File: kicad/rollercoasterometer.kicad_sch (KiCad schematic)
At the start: 15 parts, among them J101 USB_C_Receptacle, J120 STANDOFF, J125 STANDOFF, J127 STANDOFF, J129 STANDOFF, U104 Teensy4.1

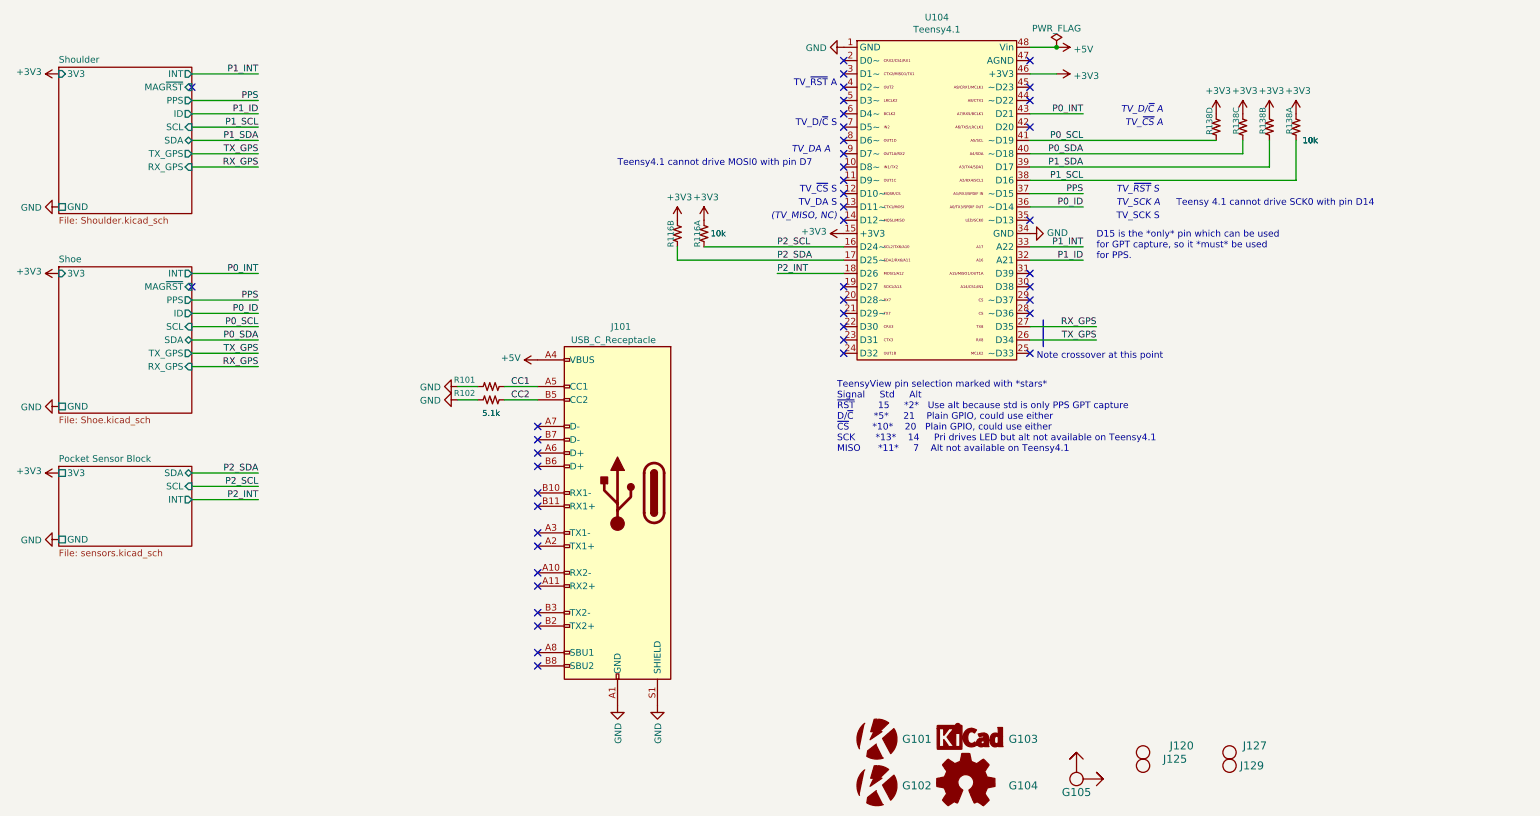
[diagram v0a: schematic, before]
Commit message: Added reference to TeensyView
TeensyView does not get a footprint because it mounts on top of the Teensy, but it is hooked up to the schematic properly.
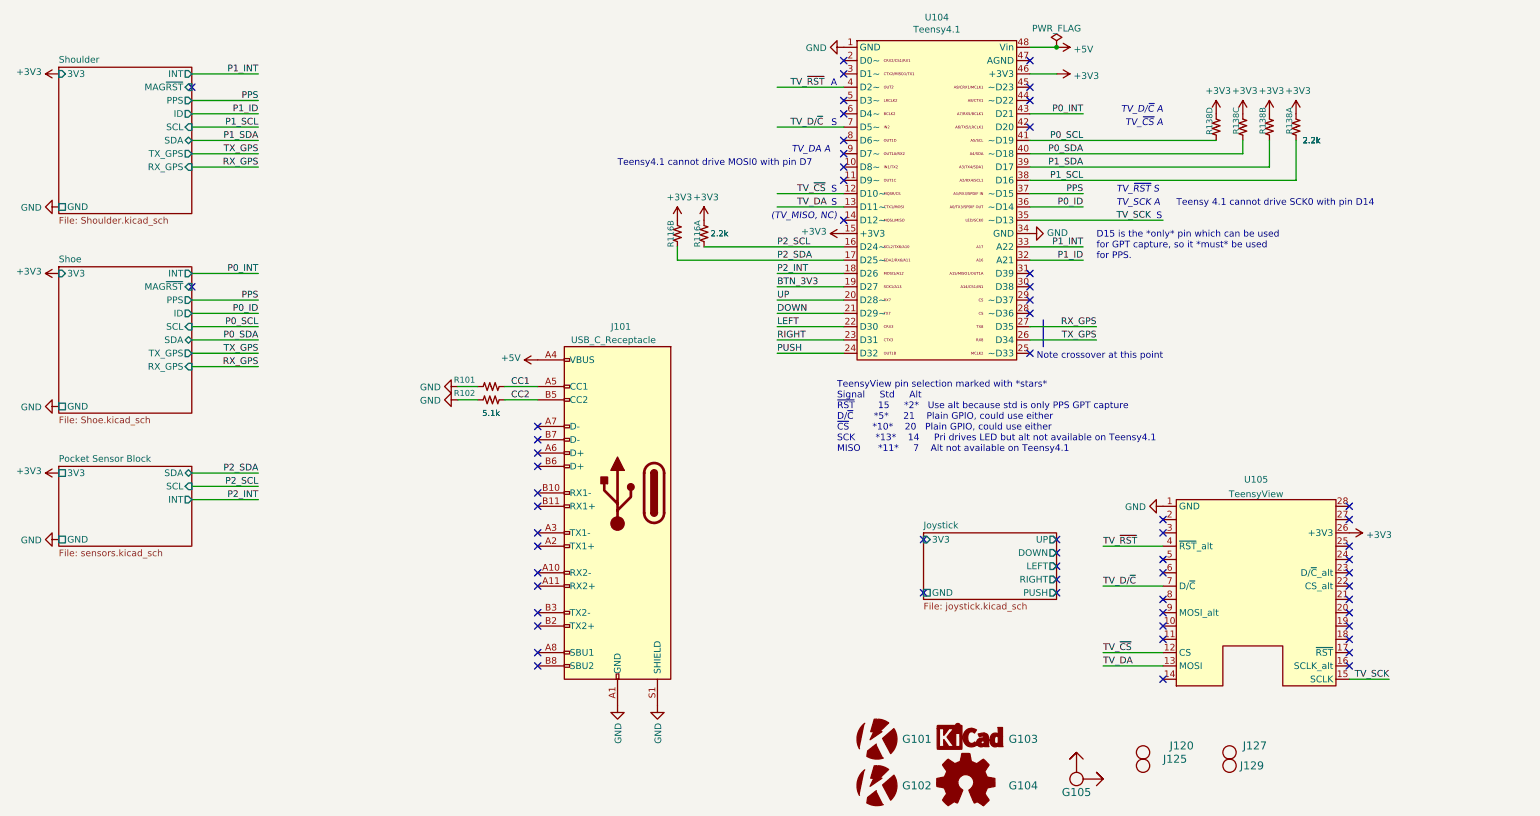
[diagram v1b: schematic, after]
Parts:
- added U105: TeensyView, symbol KwanSystems:TeensyView
- R116: value 10k -> 2.2k; Digikey 742C043103JPCT-ND -> Y5222CT-ND
- R138: value 10k -> 2.2k; Digikey 741C083103JPCT-ND -> Y7222CT-ND
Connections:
- net +3V3: now also U105.26 (+3V3)
- net GND: now also U105.1 (GND)
- net TV_~{CS}: now reaches U104.12 (D10~)
- net TV_~{CS}: now also U105.12 (CS)
- net TV_DA: now reaches U104.13 (D11~)
- net TV_DA: now also U105.13 (MOSI)
- net BTN_3V3: now reaches U104.19 (D27)
- net UP: now reaches U104.20 (D28~)
- net DOWN: now reaches U104.21 (D29~)
- net LEFT: now reaches U104.22 (D30)
- net RIGHT: now reaches U104.23 (D31)
- net PUSH: now reaches U104.24 (D32)
- net TV_SCK: now reaches U104.35 (~D13)
- net TV_SCK: now also U105.15 (SCLK)
- net TV_~{RST}: now reaches U104.4 (D2~)
- net TV_~{RST}: now also U105.4 (~{RST}_alt)
- net TV_D/~{C}: now reaches U104.7 (D5~)
- net TV_D/~{C}: now also U105.7 (D/~{C})
- no-connect marks 45 -> 62
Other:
- added sheet Joystick (joystick.kicad_sch)
- note added: "A"
- note added: "S"
- note removed: "TV_D/~{C} S"
- note removed: "TV_DA S"
- note removed: "TV_SCK S"
- note removed: "TV_~{CS} S"
- note removed: "TV_~{RST} A"

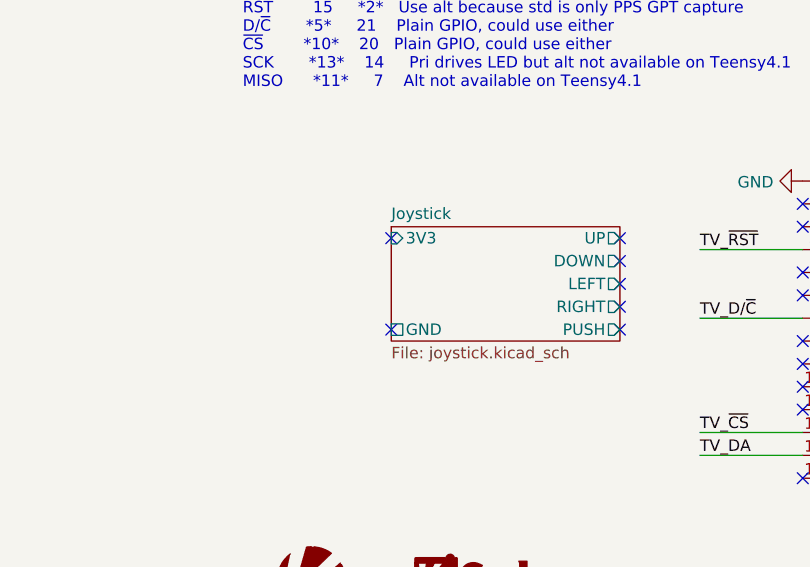
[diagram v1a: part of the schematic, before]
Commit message: Replaced JS5208 with smaller JS1400
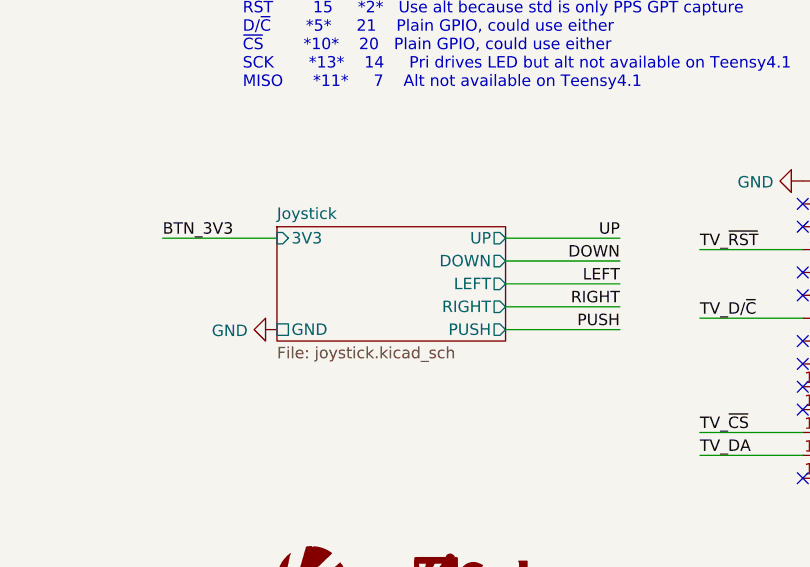
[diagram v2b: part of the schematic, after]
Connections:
- no-connect marks 62 -> 55
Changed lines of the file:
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@@
   (no_connect (at 116.84 115.57))
   (no_connect (at 175.26 43.18))
-  (no_connect (at 215.9 114.3))
-  (no_connect (at 215.9 116.84))
-  (no_connect (at 215.9 119.38))
-  (no_connect (at 215.9 121.92))
-  (no_connect (at 215.9 124.46))
-  (no_connect (at 190.5 124.46))
-  (no_connect (at 190.5 114.3))
   (no_connect (at 175.26 25.4))
   (no_connect (at 236.22 110.49))
@@
     (stroke (width 0) (type default) (color 0 0 0 0))
   )
+  (wire (pts (xy 215.9 114.3) (xy 203.2 114.3))
+    (stroke (width 0) (type default) (color 0 0 0 0))
+  )
   (wire (pts (xy 50.8 81.28) (xy 63.5 81.28))
     (stroke (width 0) (type default) (color 0 0 0 0))
@@
     (stroke (width 0) (type default) (color 0 0 0 0))
   )
+  (wire (pts (xy 215.9 116.84) (xy 203.2 116.84))
+    (stroke (width 0) (type default) (color 0 0 0 0))
+  )
   (wire (pts (xy 101.6 87.63) (xy 105.41 87.63))
     (stroke (width 0) (type default) (color 0 0 0 0))
@@
     (stroke (width 0) (type default) (color 0 0 0 0))
   )
+  (wire (pts (xy 215.9 121.92) (xy 203.2 121.92))
+    (stroke (width 0) (type default) (color 0 0 0 0))
+  )
   (wire (pts (xy 101.6 85.09) (xy 105.41 85.09))
     (stroke (width 0) (type default) (color 0 0 0 0))
@@
     (stroke (width 0) (type default) (color 0 0 0 0))
   )
+  (wire (pts (xy 215.9 124.46) (xy 203.2 124.46))
+    (stroke (width 0) (type default) (color 0 0 0 0))
+  )
   (wire (pts (xy 224.79 123.19) (xy 236.22 123.19))
     (stroke (width 0) (type default) (color 0 0 0 0))
@@
     (stroke (width 0) (type default) (color 0 0 0 0))
   )
+  (wire (pts (xy 215.9 119.38) (xy 203.2 119.38))
+    (stroke (width 0) (type default) (color 0 0 0 0))
+  )
   (wire (pts (xy 50.8 68.58) (xy 63.5 68.58))
     (stroke (width 0) (type default) (color 0 0 0 0))
@@
   )
   (wire (pts (xy 50.8 76.2) (xy 63.5 76.2))
+    (stroke (width 0) (type default) (color 0 0 0 0))
+  )
+  (wire (pts (xy 165.1 114.3) (xy 177.8 114.3))
     (stroke (width 0) (type default) (color 0 0 0 0))
   )
@@
     (effects (font (size 1.27 1.27)) (justify right bottom))
   )
+  (label "PUSH" (at 215.9 124.46 180)
+    (effects (font (size 1.27 1.27)) (justify right bottom))
+  )
   (label "RIGHT" (at 162.56 76.2 0)
     (effects (font (size 1.27 1.27)) (justify left bottom))
@@
     (effects (font (size 1.27 1.27)) (justify right bottom))
   )
+  (label "LEFT" (at 215.9 119.38 180)
+    (effects (font (size 1.27 1.27)) (justify right bottom))
+  )
   (label "TV_DA" (at 166.37 50.8 0)
     (effects (font (size 1.27 1.27)) (justify left bottom))
@@
     (effects (font (size 1.27 1.27)) (justify right bottom))
   )
+  (label "DOWN" (at 215.9 116.84 180)
+    (effects (font (size 1.27 1.27)) (justify right bottom))
+  )
   (label "PPS" (at 63.5 30.48 180)
     (effects (font (size 1.27 1.27)) (justify right bottom))
@@
     (effects (font (size 1.27 1.27)) (justify right bottom))
   )
+  (label "RIGHT" (at 215.9 121.92 180)
+    (effects (font (size 1.27 1.27)) (justify right bottom))
+  )
   (label "TX_GPS" (at 223.52 76.2 180)
     (effects (font (size 1.27 1.27)) (justify right bottom))
@@
     (effects (font (size 1.27 1.27)) (justify left bottom))
   )
+  (label "UP" (at 215.9 114.3 180)
+    (effects (font (size 1.27 1.27)) (justify right bottom))
+  )
   (label "RX_GPS" (at 63.5 43.18 180)
     (effects (font (size 1.27 1.27)) (justify right bottom))
@@
   (label "PPS" (at 63.5 68.58 180)
     (effects (font (size 1.27 1.27)) (justify right bottom))
+  )
+  (label "BTN_3V3" (at 165.1 114.3 0)
+    (effects (font (size 1.27 1.27)) (justify left bottom))
   )
   (label "P0_INT" (at 63.5 63.5 180)
@@
       (effects (font (size 1.524 1.524)) hide)
     )
+  )
+  (symbol (lib_id "power:GND") (at 177.8 124.46 270) (unit 1)
+    (in_bom yes) (on_board yes)
+    (property "Reference" "#PWR0125" (id 0) (at 171.45 124.46 0)
+      (effects (font (size 1.27 1.27)) hide)
+    )
+    (property "Value" "GND" (id 1) (at 174.5488 124.587 90)
+      (effects (font (size 1.27 1.27)) (justify right))
+    )
+    (property "Footprint" "" (id 2) (at 177.8 124.46 0)
+      (effects (font (size 1.27 1.27)) hide)
+    )
+    (property "Datasheet" "" (id 3) (at 177.8 124.46 0)
+      (effects (font (size 1.27 1.27)) hide)
+    )
+    (pin "1")
   )
   (symbol (lib_id "power:+3V3") (at 175.26 55.88 90) (unit 1)
@@
     )
   )
-  (sheet (at 190.5 113.03) (size 25.4 12.7) (fields_autoplaced)
+  (sheet (at 177.8 113.03) (size 25.4 12.7) (fields_autoplaced)
     (stroke (width 0.1524) (type solid) (color 0 0 0 0))
     (fill (color 0 0 0 0.0000))
-    (property "Sheet name" "Joystick" (id 0) (at 190.5 112.3184 0)
+    (property "Sheet name" "Joystick" (id 0) (at 177.8 112.3184 0)
       (effects (font (size 1.27 1.27)) (justify left bottom))
     )
-    (property "Sheet file" "joystick.kicad_sch" (id 1) (at 190.5 126.3146 0)
+    (property "Sheet file" "joystick.kicad_sch" (id 1) (at 177.8 126.3146 0)
       (effects (font (size 1.27 1.27)) (justify left top))
     )
-    (pin "PUSH" output (at 215.9 124.46 0)
-      (effects (font (size 1.27 1.27)) (justify right))
-    )
-    (pin "RIGHT" output (at 215.9 121.92 0)
-      (effects (font (size 1.27 1.27)) (justify right))
-    )
-    (pin "GND" passive (at 190.5 124.46 180)
+    (pin "PUSH" output (at 203.2 124.46 0)
+      (effects (font (size 1.27 1.27)) (justify right))
+    )
+    (pin "RIGHT" output (at 203.2 121.92 0)
+      (effects (font (size 1.27 1.27)) (justify right))
+    )
+    (pin "GND" passive (at 177.8 124.46 180)
       (effects (font (size 1.27 1.27)) (justify left))
     )
-    (pin "UP" output (at 215.9 114.3 0)
-      (effects (font (size 1.27 1.27)) (justify right))
-    )
-    (pin "DOWN" output (at 215.9 116.84 0)
-      (effects (font (size 1.27 1.27)) (justify right))
-    )
-    (pin "LEFT" output (at 215.9 119.38 0)
-      (effects (font (size 1.27 1.27)) (justify right))
-    )
-    (pin "3V3" input (at 190.5 114.3 180)
+    (pin "UP" output (at 203.2 114.3 0)
+      (effects (font (size 1.27 1.27)) (justify right))
+    )
+    (pin "DOWN" output (at 203.2 116.84 0)
+      (effects (font (size 1.27 1.27)) (justify right))
+    )
+    (pin "LEFT" output (at 203.2 119.38 0)
+      (effects (font (size 1.27 1.27)) (justify right))
+    )
+    (pin "3V3" input (at 177.8 114.3 180)
       (effects (font (size 1.27 1.27)) (justify left))
     )
@@
       (reference "#PWR0124") (unit 1) (value "+3V3") (footprint "")
     )
+    (path "/12e7e1c2-6411-4724-ac51-d63cd39d4205"
+      (reference "#PWR0125") (unit 1) (value "GND") (footprint "")
+    )
     (path "/ef3523e1-1944-4a94-ac44-9b4df6bc7d84/7e5f1de1-52e8-4e90-b0e4-67c16a4896ae/cee0c464-d016-4368-b0b3-b05cd22feaff"
       (reference "B401") (unit 1) (value "ML414H") (footprint "KwanSystems:Coin_Cell_ML414H")
@@
     )
     (path "/2faa4796-f6bd-4ac2-85c9-699e2ddc070c/f59f839c-15d4-467c-94d5-aa377ab314ed"
-      (reference "S3501") (unit 1) (value "JS5208") (footprint "KwanSystems:JS5208")
+      (reference "S3501") (unit 1) (value "JS1400") (footprint "KwanSystems:JS1400")
     )
     (path "/6321da49-3889-482b-8552-92945daa3d4c"
